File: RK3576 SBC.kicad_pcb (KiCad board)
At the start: 2 copper layers, 0 parts

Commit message: Add files via upload
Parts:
- added AE1: Antenna_Shield, Connector_Coaxial:U.FL_Molex_MCRF_73412-0110_Vertical, F.Cu at (230.8, 103.9)
- added C1: 22u, Capacitor_SMD:C_0603_1608Metric, F.Cu at (189.6, 96.3)
- added C10: 47u, Capacitor_SMD:C_0805_2012Metric, F.Cu at (209.8, 99.5)
- added C100: 1u, Capacitor_SMD:C_0402_1005Metric_Pad0.74x0.62mm_HandSolder, F.Cu at (232.4, 201.0)
- added C101: 1u, Capacitor_SMD:C_0402_1005Metric_Pad0.74x0.62mm_HandSolder, F.Cu at (232.4, 203.0)
- added C102: 1u, Capacitor_SMD:C_0402_1005Metric_Pad0.74x0.62mm_HandSolder, F.Cu at (232.4, 193.1)
- added C103: 1u, Capacitor_SMD:C_0402_1005Metric_Pad0.74x0.62mm_HandSolder, F.Cu at (232.4, 195.1)
- added C104: 1n, Capacitor_SMD:C_0402_1005Metric_Pad0.74x0.62mm_HandSolder, F.Cu at (232.4, 197.0)
- added C105: 1u, Capacitor_SMD:C_0402_1005Metric_Pad0.74x0.62mm_HandSolder, F.Cu at (161.2, 162.5)
- added C106: 1u, Capacitor_SMD:C_0402_1005Metric_Pad0.74x0.62mm_HandSolder, F.Cu at (161.2, 164.4)
- added C107: 1u, Capacitor_SMD:C_0402_1005Metric_Pad0.74x0.62mm_HandSolder, F.Cu at (161.2, 166.4)
- added C108: 1u, Capacitor_SMD:C_0402_1005Metric_Pad0.74x0.62mm_HandSolder, F.Cu at (161.2, 168.4)
- added C109: 1u, Capacitor_SMD:C_0402_1005Metric_Pad0.74x0.62mm_HandSolder, F.Cu at (161.2, 170.3)
- added C11: 2.2u, Capacitor_SMD:C_0402_1005Metric, F.Cu at (206.9, 115.0)
- added C110: 1u, Capacitor_SMD:C_0402_1005Metric_Pad0.74x0.62mm_HandSolder, F.Cu at (161.2, 172.3)
- added C111: 1u, Capacitor_SMD:C_0402_1005Metric_Pad0.74x0.62mm_HandSolder, F.Cu at (164.4, 162.5)
- added C112: 1u, Capacitor_SMD:C_0402_1005Metric_Pad0.74x0.62mm_HandSolder, F.Cu at (164.4, 164.4)
- added C113: 1u, Capacitor_SMD:C_0402_1005Metric_Pad0.74x0.62mm_HandSolder, F.Cu at (164.4, 166.4)
- added C114: 1u, Capacitor_SMD:C_0402_1005Metric_Pad0.74x0.62mm_HandSolder, F.Cu at (164.4, 168.4)
- added C115: 1u, Capacitor_SMD:C_0402_1005Metric_Pad0.74x0.62mm_HandSolder, F.Cu at (234.5, 140.4)
- added C116: 1u, Capacitor_SMD:C_0402_1005Metric_Pad0.74x0.62mm_HandSolder, F.Cu at (234.5, 142.3)
- added C117: 1u, Capacitor_SMD:C_0402_1005Metric_Pad0.74x0.62mm_HandSolder, F.Cu at (234.5, 144.3)
- added C118: 1u, Capacitor_SMD:C_0402_1005Metric_Pad0.74x0.62mm_HandSolder, F.Cu at (231.1, 162.9)
- added C119: 1u, Capacitor_SMD:C_0402_1005Metric_Pad0.74x0.62mm_HandSolder, F.Cu at (231.1, 164.8)
- added C12: 22u, Capacitor_SMD:C_0603_1608Metric, F.Cu at (193.6, 96.3)
- added C120: 1u, Capacitor_SMD:C_0201_0603Metric_Pad0.64x0.40mm_HandSolder, F.Cu at (127.8, 157.1)
- added C121: 1u, Capacitor_SMD:C_0402_1005Metric, F.Cu at (124.9, 150.8)
- added C122: 1u, Capacitor_SMD:C_0402_1005Metric, F.Cu at (124.9, 152.8)
- added C123: 22u, Capacitor_SMD:C_0603_1608Metric, F.Cu at (121.5, 151.1)
- added C124: 22u, Capacitor_SMD:C_0603_1608Metric, F.Cu at (121.5, 153.6)
- added C125: 22u, Capacitor_SMD:C_0603_1608Metric, F.Cu at (121.5, 156.1)
- added C126: 1u, Capacitor_SMD:C_0201_0603Metric_Pad0.64x0.40mm_HandSolder, F.Cu at (127.8, 158.8)
- added C127: 1u, Capacitor_SMD:C_0402_1005Metric, F.Cu at (124.9, 154.8)
- added C128: 1u, Capacitor_SMD:C_0402_1005Metric, F.Cu at (124.9, 156.8)
- added C129: 22u, Capacitor_SMD:C_0603_1608Metric, F.Cu at (121.5, 158.6)
- added C13: 22u, Capacitor_SMD:C_0603_1608Metric, F.Cu at (193.6, 98.8)
- added C130: 22u, Capacitor_SMD:C_0603_1608Metric, F.Cu at (121.5, 161.2)
- added C131: 22u, Capacitor_SMD:C_0603_1608Metric, F.Cu at (121.5, 163.7)
- added C132: 1u, Capacitor_SMD:C_0402_1005Metric, F.Cu at (124.9, 158.7)
- added C133: 1u, Capacitor_SMD:C_0402_1005Metric, F.Cu at (124.9, 160.7)
- added C134: 1u, Capacitor_SMD:C_0402_1005Metric, F.Cu at (124.9, 162.7)
- added C135: 1u, Capacitor_SMD:C_0402_1005Metric_Pad0.74x0.62mm_HandSolder, F.Cu at (222.0, 193.1)
- added C136: 1u, Capacitor_SMD:C_0402_1005Metric_Pad0.74x0.62mm_HandSolder, F.Cu at (222.0, 195.1)
- added C137: 1u, Capacitor_SMD:C_0402_1005Metric_Pad0.74x0.62mm_HandSolder, F.Cu at (222.0, 197.0)
- added C138: 1u, Capacitor_SMD:C_0402_1005Metric_Pad0.74x0.62mm_HandSolder, F.Cu at (222.0, 199.0)
- added C139: 1u, Capacitor_SMD:C_0402_1005Metric_Pad0.74x0.62mm_HandSolder, F.Cu at (222.0, 201.0)
- added C14: 22u, Capacitor_SMD:C_0603_1608Metric, F.Cu at (193.6, 101.3)
- added C140: 1u, Capacitor_SMD:C_0402_1005Metric_Pad0.74x0.62mm_HandSolder, F.Cu at (222.0, 202.9)
- added C141: 18pF, Capacitor_SMD:C_0402_1005Metric_Pad0.74x0.62mm_HandSolder, F.Cu at (222.0, 204.9)
- added C142: 18pF, Capacitor_SMD:C_0402_1005Metric_Pad0.74x0.62mm_HandSolder, F.Cu at (222.0, 206.9)
- added C143: 1u, Capacitor_SMD:C_0402_1005Metric_Pad0.74x0.62mm_HandSolder, F.Cu at (133.4, 160.7)
- added C144: 10u, Capacitor_SMD:C_0402_1005Metric_Pad0.74x0.62mm_HandSolder, F.Cu at (231.1, 150.9)
- added C145: 1u, Capacitor_SMD:C_0402_1005Metric_Pad0.74x0.62mm_HandSolder, F.Cu at (231.1, 152.8)
- added C146: 10u, Capacitor_SMD:C_0402_1005Metric_Pad0.74x0.62mm_HandSolder, F.Cu at (231.1, 154.8)
- added C147: 1u, Capacitor_SMD:C_0402_1005Metric_Pad0.74x0.62mm_HandSolder, F.Cu at (231.1, 156.8)
- added C148: 1u, Capacitor_SMD:C_0402_1005Metric_Pad0.74x0.62mm_HandSolder, F.Cu at (129.2, 199.3)
- added C149: 1u, Capacitor_SMD:C_0402_1005Metric_Pad0.74x0.62mm_HandSolder, F.Cu at (129.2, 201.3)
- added C15: 47u, Capacitor_SMD:C_0805_2012Metric, F.Cu at (209.8, 102.5)
- added C150: 1u, Capacitor_SMD:C_0402_1005Metric_Pad0.74x0.62mm_HandSolder, F.Cu at (129.2, 203.2)
- added C151: 1u, Capacitor_SMD:C_0402_1005Metric_Pad0.74x0.62mm_HandSolder, F.Cu at (129.2, 205.2)
- added C152: 1u, Capacitor_SMD:C_0402_1005Metric_Pad0.74x0.62mm_HandSolder, F.Cu at (129.2, 207.2)
- added C153: 1u, Capacitor_SMD:C_0402_1005Metric_Pad0.74x0.62mm_HandSolder, F.Cu at (129.2, 209.2)
- added C154: 1u, Capacitor_SMD:C_0402_1005Metric_Pad0.74x0.62mm_HandSolder, F.Cu at (132.4, 199.3)
- added C155: 1u, Capacitor_SMD:C_0402_1005Metric_Pad0.74x0.62mm_HandSolder, F.Cu at (132.4, 201.3)
- added C156: 1u, Capacitor_SMD:C_0402_1005Metric_Pad0.74x0.62mm_HandSolder, F.Cu at (132.4, 203.2)
- added C157: 1u, Capacitor_SMD:C_0402_1005Metric_Pad0.74x0.62mm_HandSolder, F.Cu at (132.4, 205.2)
- added C158: 1u, Capacitor_SMD:C_0402_1005Metric_Pad0.74x0.62mm_HandSolder, F.Cu at (132.4, 207.2)
- added C159: 1u, Capacitor_SMD:C_0402_1005Metric_Pad0.74x0.62mm_HandSolder, F.Cu at (133.4, 150.8)
- added C16: 2.2u, Capacitor_SMD:C_0402_1005Metric, F.Cu at (206.9, 117.0)
- added C160: 1u, Capacitor_SMD:C_0402_1005Metric_Pad0.74x0.62mm_HandSolder, F.Cu at (133.4, 152.8)
- added C161: 1u, Capacitor_SMD:C_0402_1005Metric_Pad0.74x0.62mm_HandSolder, F.Cu at (133.4, 154.8)
- added C162: 1u, Capacitor_SMD:C_0402_1005Metric_Pad0.74x0.62mm_HandSolder, F.Cu at (133.4, 156.8)
- added C163: 1u, Capacitor_SMD:C_0402_1005Metric_Pad0.74x0.62mm_HandSolder, F.Cu at (129.7, 193.0)
- added C164: 22u, Capacitor_SMD:C_0603_1608Metric, F.Cu at (130.0, 190.7)
- added C165: 1u, Capacitor_SMD:C_0201_0603Metric_Pad0.64x0.40mm_HandSolder, F.Cu at (142.7, 194.9)
- added C166: 1u, Capacitor_SMD:C_0201_0603Metric_Pad0.64x0.40mm_HandSolder, F.Cu at (142.7, 196.6)
- added C167: 1u, Capacitor_SMD:C_0201_0603Metric_Pad0.64x0.40mm_HandSolder, F.Cu at (142.7, 198.4)
- added C168: 200p, Capacitor_SMD:C_0402_1005Metric_Pad0.74x0.62mm_HandSolder, F.Cu at (151.6, 203.7)
- added C169: 200p, Capacitor_SMD:C_0402_1005Metric_Pad0.74x0.62mm_HandSolder, F.Cu at (151.6, 205.7)
- added C17: 22u, Capacitor_SMD:C_0603_1608Metric, F.Cu at (193.6, 103.8)
- added C170: 100n, Capacitor_SMD:C_0201_0603Metric_Pad0.64x0.40mm_HandSolder, F.Cu at (142.7, 200.1)
- added C171: 100n, Capacitor_SMD:C_0201_0603Metric_Pad0.64x0.40mm_HandSolder, F.Cu at (142.7, 201.9)
- added C172: 100n, Capacitor_SMD:C_0201_0603Metric_Pad0.64x0.40mm_HandSolder, F.Cu at (145.5, 194.9)
- added C173: 100n, Capacitor_SMD:C_0201_0603Metric_Pad0.64x0.40mm_HandSolder, F.Cu at (145.5, 196.6)
- added C174: 100n, Capacitor_SMD:C_0201_0603Metric_Pad0.64x0.40mm_HandSolder, F.Cu at (145.5, 198.4)
- added C175: 100n, Capacitor_SMD:C_0201_0603Metric_Pad0.64x0.40mm_HandSolder, F.Cu at (145.5, 200.1)
- added C176: 100n, Capacitor_SMD:C_0201_0603Metric_Pad0.64x0.40mm_HandSolder, F.Cu at (145.5, 201.9)
- added C177: 100n, Capacitor_SMD:C_0201_0603Metric_Pad0.64x0.40mm_HandSolder, F.Cu at (148.3, 194.9)
- added C178: 100n, Capacitor_SMD:C_0201_0603Metric_Pad0.64x0.40mm_HandSolder, F.Cu at (148.3, 196.6)
- added C179: 100n, Capacitor_SMD:C_0201_0603Metric_Pad0.64x0.40mm_HandSolder, F.Cu at (148.3, 198.4)
- added C18: 22u, Capacitor_SMD:C_0603_1608Metric, F.Cu at (193.6, 106.3)
- added C180: 1u, Capacitor_SMD:C_0402_1005Metric_Pad0.74x0.62mm_HandSolder, F.Cu at (160.5, 129.4)
- added C181: 22u, Capacitor_SMD:C_0603_1608Metric, F.Cu at (151.7, 201.0)
- added C182: 22u, Capacitor_SMD:C_0603_1608Metric, F.Cu at (169.3, 115.8)
- added C183: 1u, Capacitor_SMD:C_0402_1005Metric_Pad0.74x0.62mm_HandSolder, F.Cu at (151.6, 207.7)
- added C184: 100n, Capacitor_SMD:C_0201_0603Metric_Pad0.64x0.40mm_HandSolder, F.Cu at (160.3, 115.4)
- added C185: 100n, Capacitor_SMD:C_0201_0603Metric_Pad0.64x0.40mm_HandSolder, F.Cu at (160.3, 117.1)
- added C186: 100n, Capacitor_SMD:C_0201_0603Metric_Pad0.64x0.40mm_HandSolder, F.Cu at (160.3, 118.9)
- added C187: 100n, Capacitor_SMD:C_0201_0603Metric_Pad0.64x0.40mm_HandSolder, F.Cu at (160.3, 120.6)
- added C188: 100n, Capacitor_SMD:C_0201_0603Metric_Pad0.64x0.40mm_HandSolder, F.Cu at (160.3, 122.4)
- added C189: 100n, Capacitor_SMD:C_0201_0603Metric_Pad0.64x0.40mm_HandSolder, F.Cu at (160.3, 124.1)
- added C19: 22u, Capacitor_SMD:C_0603_1608Metric, F.Cu at (193.6, 108.8)
- added C190: 100n, Capacitor_SMD:C_0201_0603Metric_Pad0.64x0.40mm_HandSolder, F.Cu at (163.1, 115.4)
- added C191: 100n, Capacitor_SMD:C_0201_0603Metric_Pad0.64x0.40mm_HandSolder, F.Cu at (163.1, 117.1)
- added C196: 100n, Capacitor_SMD:C_0201_0603Metric_Pad0.64x0.40mm_HandSolder, F.Cu at (163.1, 118.9)
- added C197: 100n, Capacitor_SMD:C_0201_0603Metric_Pad0.64x0.40mm_HandSolder, F.Cu at (163.1, 120.6)
- added C198: 100n, Capacitor_SMD:C_0201_0603Metric_Pad0.64x0.40mm_HandSolder, F.Cu at (163.1, 122.4)
- added C199: 100n, Capacitor_SMD:C_0201_0603Metric_Pad0.64x0.40mm_HandSolder, F.Cu at (163.1, 124.1)
- added C2: 22u, Capacitor_SMD:C_0603_1608Metric, F.Cu at (189.6, 98.8)
- added C20: 47u, Capacitor_SMD:C_0805_2012Metric, F.Cu at (209.8, 105.5)
- added C200: 100n, Capacitor_SMD:C_0201_0603Metric_Pad0.64x0.40mm_HandSolder, F.Cu at (165.9, 115.4)
- added C201: 100n, Capacitor_SMD:C_0201_0603Metric_Pad0.64x0.40mm_HandSolder, F.Cu at (165.9, 117.1)
- added C202: 100n, Capacitor_SMD:C_0201_0603Metric_Pad0.64x0.40mm_HandSolder, F.Cu at (165.9, 118.9)
- added C203: 100n, Capacitor_SMD:C_0201_0603Metric_Pad0.64x0.40mm_HandSolder, F.Cu at (165.9, 120.6)
- added C204: 1u, Capacitor_SMD:C_0201_0603Metric_Pad0.64x0.40mm_HandSolder, F.Cu at (199.5, 169.6)
- added C205: 1u, Capacitor_SMD:C_0201_0603Metric_Pad0.64x0.40mm_HandSolder, F.Cu at (199.5, 171.4)
- added C206: 1u, Capacitor_SMD:C_0201_0603Metric_Pad0.64x0.40mm_HandSolder, F.Cu at (199.5, 173.1)
- added C207: 1u, Capacitor_SMD:C_0201_0603Metric_Pad0.64x0.40mm_HandSolder, F.Cu at (199.5, 174.9)
- added C208: 10u, Capacitor_SMD:C_0603_1608Metric, F.Cu at (208.5, 181.3)
- added C209: 1u, Capacitor_SMD:C_0201_0603Metric_Pad0.64x0.40mm_HandSolder, F.Cu at (199.5, 176.6)
- added C21: 2.2u, Capacitor_SMD:C_0402_1005Metric, F.Cu at (206.9, 118.9)
- added C210: 10u, Capacitor_SMD:C_0603_1608Metric, F.Cu at (208.5, 183.8)
- added C211: 1u, Capacitor_SMD:C_0201_0603Metric_Pad0.64x0.40mm_HandSolder, F.Cu at (199.5, 178.4)
- added C212: 1u, Capacitor_SMD:C_0201_0603Metric_Pad0.64x0.40mm_HandSolder, F.Cu at (199.5, 180.1)
- added C213: 1u, Capacitor_SMD:C_0201_0603Metric_Pad0.64x0.40mm_HandSolder, F.Cu at (202.3, 169.6)
- added C214: 1u, Capacitor_SMD:C_0201_0603Metric_Pad0.64x0.40mm_HandSolder, F.Cu at (202.3, 171.4)
- added C215: 1u, Capacitor_SMD:C_0201_0603Metric_Pad0.64x0.40mm_HandSolder, F.Cu at (202.3, 173.1)
- added C216: 1u, Capacitor_SMD:C_0201_0603Metric_Pad0.64x0.40mm_HandSolder, F.Cu at (202.3, 174.9)
- added C217: 1u, Capacitor_SMD:C_0201_0603Metric_Pad0.64x0.40mm_HandSolder, F.Cu at (202.3, 176.6)
- added C218: 1u, Capacitor_SMD:C_0201_0603Metric_Pad0.64x0.40mm_HandSolder, F.Cu at (202.3, 178.4)
- added C219: 1u, Capacitor_SMD:C_0201_0603Metric_Pad0.64x0.40mm_HandSolder, F.Cu at (202.3, 180.1)
- added C22: 2.2u, Capacitor_SMD:C_0402_1005Metric, F.Cu at (206.9, 120.9)
- added C220: 1u, Capacitor_SMD:C_0201_0603Metric_Pad0.64x0.40mm_HandSolder, F.Cu at (205.1, 169.6)
- added C221: 1u, Capacitor_SMD:C_0201_0603Metric_Pad0.64x0.40mm_HandSolder, F.Cu at (205.1, 171.4)
- added C222: 1u, Capacitor_SMD:C_0201_0603Metric_Pad0.64x0.40mm_HandSolder, F.Cu at (205.1, 173.1)
- added C223: 10u, Capacitor_SMD:C_0603_1608Metric, F.Cu at (208.5, 186.3)
- added C224: 10u, Capacitor_SMD:C_0603_1608Metric, F.Cu at (208.5, 188.9)
- added C225: 1u, Capacitor_SMD:C_0201_0603Metric_Pad0.64x0.40mm_HandSolder, F.Cu at (205.1, 174.9)
- added C226: 1u, Capacitor_SMD:C_0201_0603Metric_Pad0.64x0.40mm_HandSolder, F.Cu at (205.1, 176.6)
- added C227: 20pF, Capacitor_SMD:C_0402_1005Metric_Pad0.74x0.62mm_HandSolder, F.Cu at (215.2, 184.8)
- added C228: 20pF, Capacitor_SMD:C_0402_1005Metric_Pad0.74x0.62mm_HandSolder, F.Cu at (215.2, 186.8)
- added C229: 1u, Capacitor_SMD:C_0201_0603Metric_Pad0.64x0.40mm_HandSolder, F.Cu at (143.7, 140.3)
- added C23: 2.2u, Capacitor_SMD:C_0402_1005Metric, F.Cu at (209.7, 111.0)
- added C230: 1u, Capacitor_SMD:C_0201_0603Metric_Pad0.64x0.40mm_HandSolder, F.Cu at (143.7, 142.0)
- added C231: 1u, Capacitor_SMD:C_0201_0603Metric_Pad0.64x0.40mm_HandSolder, F.Cu at (143.7, 143.8)
- added C232: 1u, Capacitor_SMD:C_0201_0603Metric_Pad0.64x0.40mm_HandSolder, F.Cu at (143.7, 145.5)
- added C233: 1u, Capacitor_SMD:C_0201_0603Metric_Pad0.64x0.40mm_HandSolder, F.Cu at (143.7, 147.3)
- added C234: 1u, Capacitor_SMD:C_0201_0603Metric_Pad0.64x0.40mm_HandSolder, F.Cu at (143.7, 149.0)
- added C235: 1u, Capacitor_SMD:C_0201_0603Metric_Pad0.64x0.40mm_HandSolder, F.Cu at (143.7, 150.8)
- added C236: 1u, Capacitor_SMD:C_0201_0603Metric_Pad0.64x0.40mm_HandSolder, F.Cu at (143.7, 152.5)
- added C237: 1u, Capacitor_SMD:C_0201_0603Metric_Pad0.64x0.40mm_HandSolder, F.Cu at (143.7, 154.3)
- added C238: 1u, Capacitor_SMD:C_0201_0603Metric_Pad0.64x0.40mm_HandSolder, F.Cu at (143.7, 156.0)
- added C239: 1u, Capacitor_SMD:C_0201_0603Metric_Pad0.64x0.40mm_HandSolder, F.Cu at (143.7, 157.8)
- added C24: 2.2u, Capacitor_SMD:C_0402_1005Metric, F.Cu at (209.7, 113.0)
- added C240: 22u, Capacitor_SMD:C_0603_1608Metric, F.Cu at (140.3, 140.6)
- added C241: 22u, Capacitor_SMD:C_0603_1608Metric, F.Cu at (140.3, 143.2)
- added C242: 22u, Capacitor_SMD:C_0603_1608Metric, F.Cu at (140.3, 145.7)
- added C243: 1u, Capacitor_SMD:C_0201_0603Metric_Pad0.64x0.40mm_HandSolder, F.Cu at (146.5, 140.3)
- added C244: 1u, Capacitor_SMD:C_0201_0603Metric_Pad0.64x0.40mm_HandSolder, F.Cu at (146.5, 142.0)
- added C245: 1u, Capacitor_SMD:C_0201_0603Metric_Pad0.64x0.40mm_HandSolder, F.Cu at (146.5, 143.8)
- added C246: 1u, Capacitor_SMD:C_0201_0603Metric_Pad0.64x0.40mm_HandSolder, F.Cu at (146.5, 145.5)
- added C247: 1u, Capacitor_SMD:C_0201_0603Metric_Pad0.64x0.40mm_HandSolder, F.Cu at (146.5, 147.3)
- added C248: 1u, Capacitor_SMD:C_0201_0603Metric_Pad0.64x0.40mm_HandSolder, F.Cu at (146.5, 149.0)
- added C249: 1u, Capacitor_SMD:C_0201_0603Metric_Pad0.64x0.40mm_HandSolder, F.Cu at (146.5, 150.8)
- added C25: 22u, Capacitor_SMD:C_0603_1608Metric, F.Cu at (197.6, 96.3)
- added C250: 1u, Capacitor_SMD:C_0201_0603Metric_Pad0.64x0.40mm_HandSolder, F.Cu at (146.5, 152.5)
- added C251: 1u, Capacitor_SMD:C_0201_0603Metric_Pad0.64x0.40mm_HandSolder, F.Cu at (146.5, 154.3)
- added C252: 1u, Capacitor_SMD:C_0201_0603Metric_Pad0.64x0.40mm_HandSolder, F.Cu at (146.5, 156.0)
- added C253: 1u, Capacitor_SMD:C_0201_0603Metric_Pad0.64x0.40mm_HandSolder, F.Cu at (146.5, 157.8)
- added C254: 1u, Capacitor_SMD:C_0201_0603Metric_Pad0.64x0.40mm_HandSolder, F.Cu at (149.3, 140.3)
- added C255: 1u, Capacitor_SMD:C_0201_0603Metric_Pad0.64x0.40mm_HandSolder, F.Cu at (149.3, 142.0)
- added C256: 1u, Capacitor_SMD:C_0201_0603Metric_Pad0.64x0.40mm_HandSolder, F.Cu at (149.3, 143.8)
- added C257: 22u, Capacitor_SMD:C_0603_1608Metric, F.Cu at (140.3, 148.2)
- added C258: 1u, Capacitor_SMD:C_0201_0603Metric_Pad0.64x0.40mm_HandSolder, F.Cu at (149.3, 145.5)
- added C259: 1u, Capacitor_SMD:C_0201_0603Metric_Pad0.64x0.40mm_HandSolder, F.Cu at (149.3, 147.3)
- added C26: 22u, Capacitor_SMD:C_0603_1608Metric, F.Cu at (197.6, 98.8)
- added C260: 1u, Capacitor_SMD:C_0201_0603Metric_Pad0.64x0.40mm_HandSolder, F.Cu at (149.3, 149.0)
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
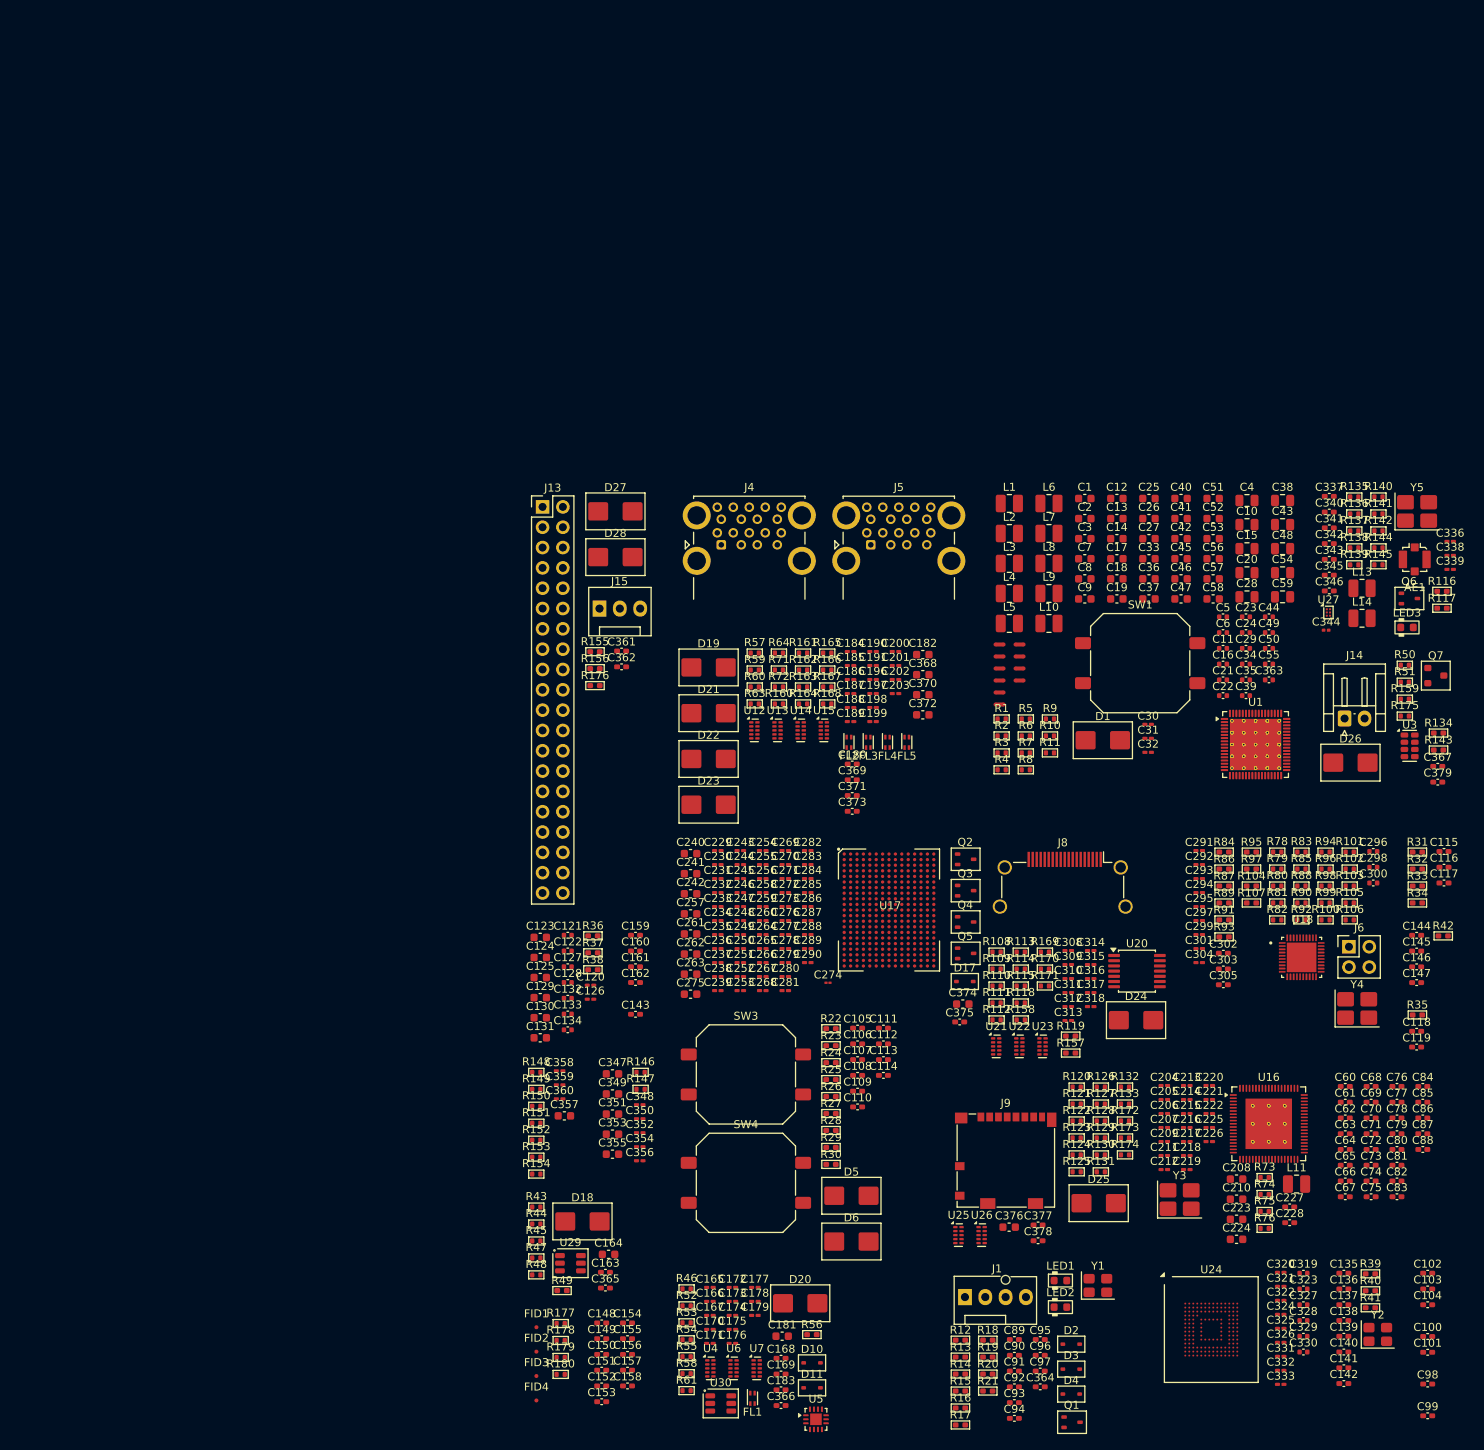
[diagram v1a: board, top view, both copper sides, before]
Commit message: SBC Board V0.2
The SBC schematics before footprint and part number check
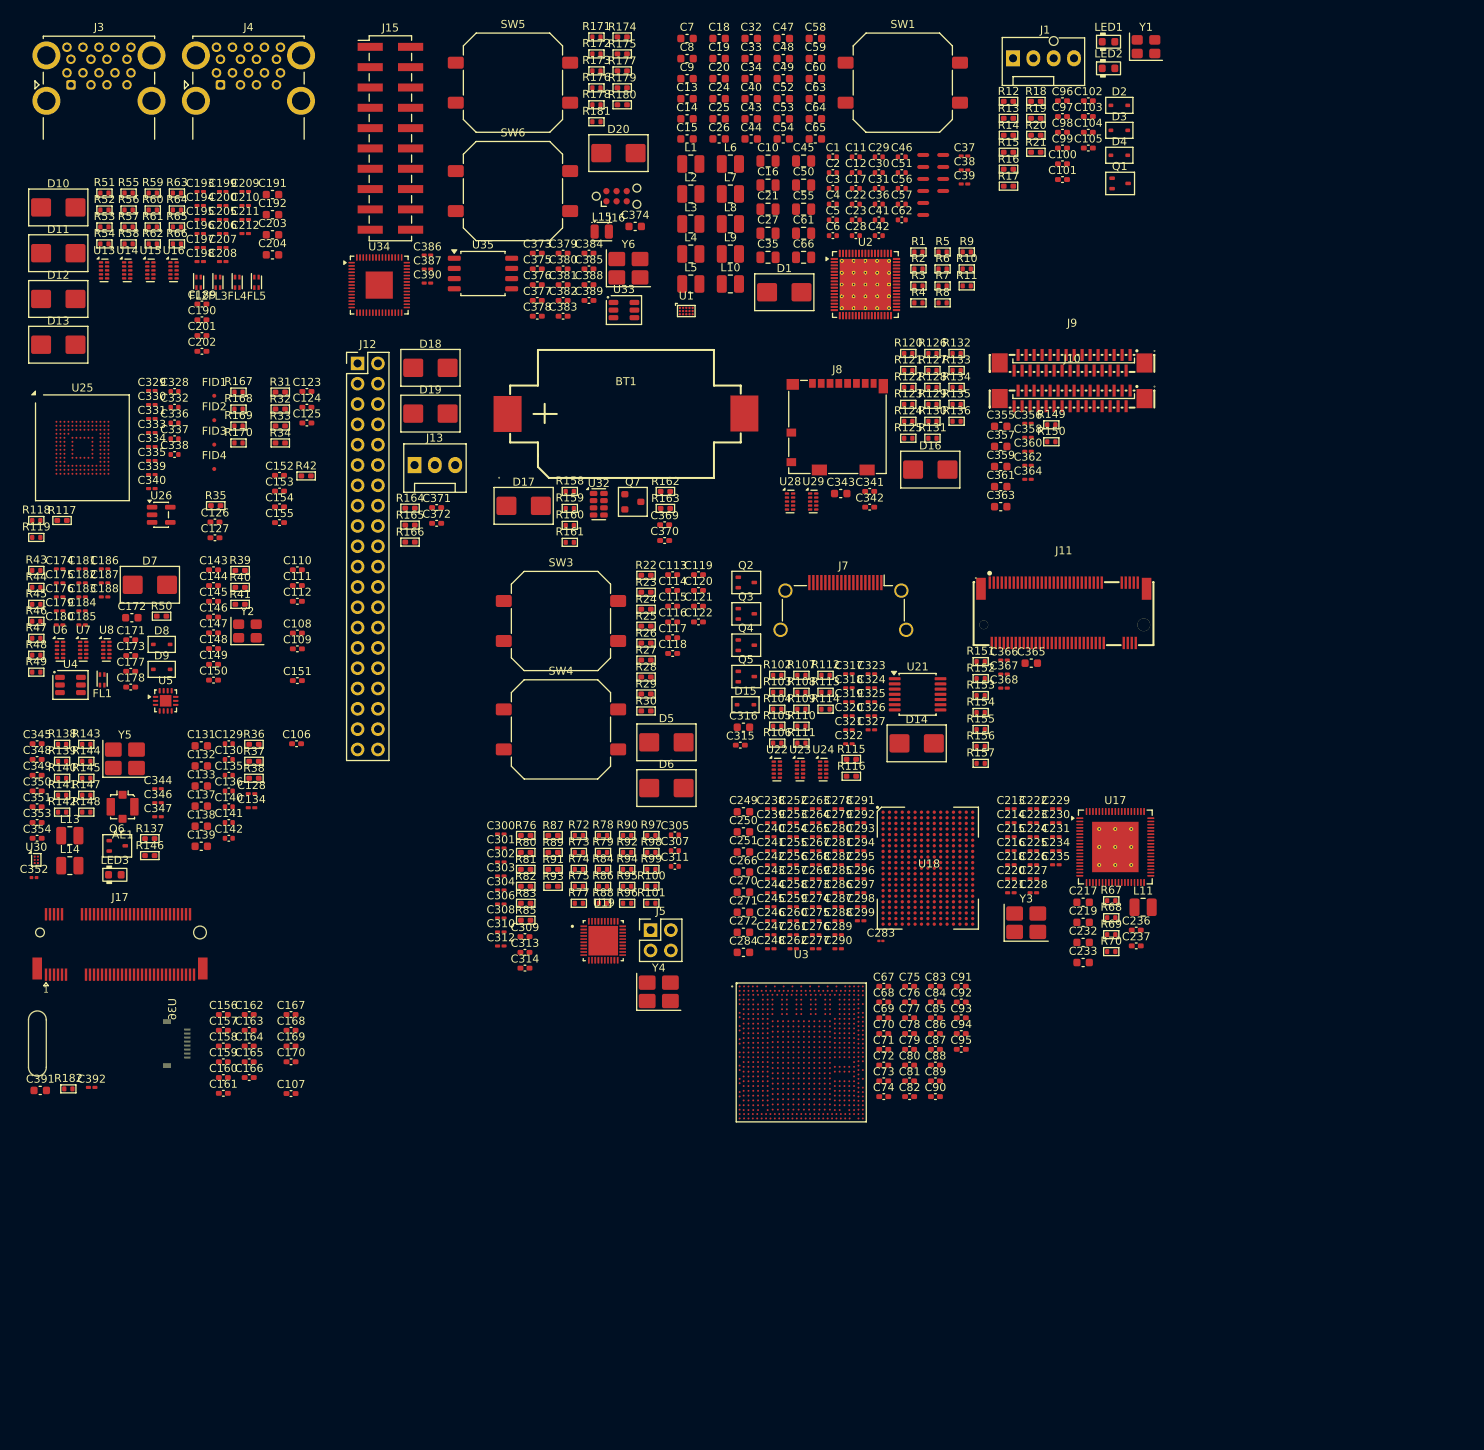
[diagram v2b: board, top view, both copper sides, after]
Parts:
- removed D21, D22, D23, D24, D25, D26, D27, D28: SMBJ5.0CA, PCM_Diode_SMD_AKL:D_SMB_TVS
- removed J14: B2B Connector, Connector_JST:JST_EH_S2B-EH_1x02_P2.50mm_Horizontal
- removed J6: POE Connector, Connector_PinHeader_2.54mm:PinHeader_2x02_P2.54mm_Vertical
- removed R71: 0R, PCM_Resistor_SMD_AKL:R_0402_1005Metric
- removed U12: TPD4E05U06DQA, Package_SON:USON-10_2.5x1.0mm_P0.5mm
- removed U20: TXB0104PW, Package_SO:TSSOP-14_4.4x5mm_P0.65mm
- removed U27: BGS12P2L6E6327XTSA1, Package_LGA:Infineon_PG-TSNP-6-10_0.7x1.1mm_0.7x1.1mm_P0.4mm
- added BT1: BS-06-B4AA012, easyeda2kicad:BAT-SMD_BS-06-B4AA012, F.Cu at (132.2, 85.7)
- added C192: 22u, Capacitor_SMD:C_0603_1608Metric, F.Cu at (88.0, 60.8)
- added C193: 100n, Capacitor_SMD:C_0201_0603Metric_Pad0.64x0.40mm_HandSolder, F.Cu at (79.0, 57.9)
- added C194: 100n, Capacitor_SMD:C_0201_0603Metric_Pad0.64x0.40mm_HandSolder, F.Cu at (79.0, 59.6)
- added C195: 100n, Capacitor_SMD:C_0201_0603Metric_Pad0.64x0.40mm_HandSolder, F.Cu at (79.0, 61.4)
- added C306: 1u, Capacitor_SMD:C_0201_0603Metric_Pad0.64x0.40mm_HandSolder, F.Cu at (116.6, 146.9)
- added C307: 10u, Capacitor_SMD:C_0402_1005Metric, F.Cu at (138.3, 140.3)
- added C334: 1u, Capacitor_SMD:C_0201_0603Metric_Pad0.64x0.40mm_HandSolder, F.Cu at (73.0, 89.8)
- added C335: 1u, Capacitor_SMD:C_0201_0603Metric_Pad0.64x0.40mm_HandSolder, F.Cu at (73.0, 91.5)
- added C380: 1u, Capacitor_SMD:C_0402_1005Metric_Pad0.74x0.62mm_HandSolder, F.Cu at (124.4, 67.6)
- added C381: 1u, Capacitor_SMD:C_0402_1005Metric_Pad0.74x0.62mm_HandSolder, F.Cu at (124.4, 69.5)
- added C382: 1u, Capacitor_SMD:C_0402_1005Metric_Pad0.74x0.62mm_HandSolder, F.Cu at (124.4, 71.5)
- added C383: 1u, Capacitor_SMD:C_0402_1005Metric_Pad0.74x0.62mm_HandSolder, F.Cu at (124.4, 73.5)
- added C384: 1u, Capacitor_SMD:C_0402_1005Metric_Pad0.74x0.62mm_HandSolder, F.Cu at (127.6, 65.6)
- added C385: 1u, Capacitor_SMD:C_0402_1005Metric_Pad0.74x0.62mm_HandSolder, F.Cu at (127.6, 67.6)
- added C386: 1u, Capacitor_SMD:C_0201_0603Metric_Pad0.64x0.40mm_HandSolder, F.Cu at (107.4, 65.8)
- added C387: 1u, Capacitor_SMD:C_0201_0603Metric_Pad0.64x0.40mm_HandSolder, F.Cu at (107.4, 67.6)
- added C388: 34pF, Capacitor_SMD:C_0402_1005Metric_Pad0.74x0.62mm_HandSolder, F.Cu at (127.6, 69.5)
- added C389: 34pF, Capacitor_SMD:C_0402_1005Metric_Pad0.74x0.62mm_HandSolder, F.Cu at (127.6, 71.5)
- added C390: 1u, Capacitor_SMD:C_0201_0603Metric_Pad0.64x0.40mm_HandSolder, F.Cu at (107.4, 69.3)
- added C391: 10u, Capacitor_SMD:C_0603_1608Metric, F.Cu at (59.0, 170.2)
- added C392: 1u, Capacitor_SMD:C_0201_0603Metric_Pad0.64x0.40mm_HandSolder, F.Cu at (65.4, 169.9)
- added D12: SMBJ5.0CA, PCM_Diode_SMD_AKL:D_SMB_TVS, F.Cu at (61.3, 71.3)
- added D13: SMBJ5.0CA, PCM_Diode_SMD_AKL:D_SMB_TVS, F.Cu at (61.3, 77.0)
- added D14: SMBJ5.0CA, PCM_Diode_SMD_AKL:D_SMB_TVS, F.Cu at (168.6, 126.9)
- added D15: PESD5V0S1BA, PCM_Diode_SMD_AKL:D_SOD-323_TVS, F.Cu at (147.2, 122.0)
- added D16: SMBJ5.0CA, PCM_Diode_SMD_AKL:D_SMB_TVS, F.Cu at (170.3, 92.6)
- added D7: SMBJ5.0CA, PCM_Diode_SMD_AKL:D_SMB_TVS, F.Cu at (72.7, 107.0)
- added D8: PESD5V0S1BA, PCM_Diode_SMD_AKL:D_SOD-323_TVS, F.Cu at (74.2, 114.5)
- added D9: PESD5V0S1BA, PCM_Diode_SMD_AKL:D_SOD-323_TVS, F.Cu at (74.2, 117.6)
- added J10: DSI Connector, easyeda2kicad:FPC-SMD_30P-L20.5-W2.0-P0.50, F.Cu at (188.0, 83.8)
- added J11: 1-2199230-5, easyeda2kicad:PCIE-SMD_75P-P0.50_1-2199230-5, F.Cu at (186.9, 110.5)
- added J12: Raspberry_Pi_4, #kicad Library:40-pin GPIO Header for Raspberry Pi, F.Cu at (98.7, 79.4)
- added J16: Conn_ARM_SWD_TagConnect_TC2030-NL, Connector:Tag-Connect_TC2030-IDC-NL_2x03_P1.27mm_Vertical, F.Cu at (131.0, 58.5)
- added J17: TE_2199230-3, Datasheet_Footprints:TE_2199230-3, F.Cu at (69.0, 150.5)
- added J3: USB3_A_Stacked, Connector_USB:USB3_A_Molex_48406-0001_Horizontal_Stacked, F.Cu at (62.8, 44.5)
- added J7: HDMI_A, Connector_Video:HDMI_A_Amphenol_10029449-x01xLF_Horizontal, F.Cu at (159.4, 111.8)
- added L15: YL201209-3R3K, Inductor_SMD:L_Coilcraft_0805HQ_2012Metric, F.Cu at (129.2, 62.9)
- added R181: 1k, PCM_Resistor_SMD_AKL:R_0402_1005Metric, F.Cu at (128.5, 49.2)
- added R182: 10k, PCM_Resistor_SMD_AKL:R_0402_1005Metric, F.Cu at (62.5, 170.1)
- added R62: 100k, PCM_Resistor_SMD_AKL:R_0402_1005Metric, F.Cu at (73.1, 64.4)
- added R65: 0R, PCM_Resistor_SMD_AKL:R_0402_1005Metric, F.Cu at (76.1, 62.3)
- added R66: 0R, PCM_Resistor_SMD_AKL:R_0402_1005Metric, F.Cu at (76.1, 64.4)
- added R67: 100k, PCM_Resistor_SMD_AKL:R_0402_1005Metric, F.Cu at (192.9, 146.5)
- added R68: 100k, PCM_Resistor_SMD_AKL:R_0402_1005Metric, F.Cu at (192.9, 148.7)
- added R69: 0R, PCM_Resistor_SMD_AKL:R_0402_1005Metric, F.Cu at (192.9, 150.8)
- added R70: 6.2k, PCM_Resistor_SMD_AKL:R_0402_1005Metric, F.Cu at (192.9, 152.9)
- added R77: 4.7k, PCM_Resistor_SMD_AKL:R_0402_1005Metric, F.Cu at (126.3, 146.8)
- added SW5: SW_Push, Button_Switch_SMD:SW_Push_1P1T_NO_CK_PTS125Sx85SMTR, F.Cu at (118.1, 44.3)
- added SW6: SW_Push, Button_Switch_SMD:SW_Push_1P1T_NO_CK_PTS125Sx85SMTR, F.Cu at (118.1, 57.8)
- added U19: RTL8211F-CG, #kicad Library:QFN40P500X500X90-41N, F.Cu at (129.4, 151.5)
- added U2: RK806S-5, Package_DFN_QFN:QFN-68-1EP_8x8mm_P0.4mm_EP6.4x6.4mm_ThermalVias, F.Cu at (162.2, 69.5)
- added U28: TPD4E05U06DQA, Package_SON:USON-10_2.5x1.0mm_P0.5mm, F.Cu at (152.7, 96.6)
- added U32: RV-3028-C7, Package_SON:MicroCrystal_C7_SON-8_1.5x3.2mm_P0.9mm, F.Cu at (128.8, 97.0)
- added U33: ETA7014S2G, PCM_Package_TO_SOT_SMD_AKL:TSOT-23-6, F.Cu at (132.0, 72.7)
- added U34: RP2350A, Package_DFN_QFN:QFN-60-1EP_7x7mm_P0.4mm_EP3.4x3.4mm, F.Cu at (101.4, 69.6)
- added U35: W25Q128JVS, Package_SO:SOIC-8_5.3x5.3mm_P1.27mm, F.Cu at (114.3, 68.1)
- added U36: 0.96 OLED Display 8 pins, Datasheet_Footprints:FFC-SMD_8P-P0.50_AFC42-S08FMA-1H_BOTTOM, F.Cu at (75.5, 164.4)
- added U8: TPD4E05U06DQA, Package_SON:USON-10_2.5x1.0mm_P0.5mm, F.Cu at (67.3, 115.2)
- added Y6: TAXM12M4RLBDDT2T, Crystal:Crystal_SMD_3225-4Pin_3.2x2.5mm_HandSoldering, F.Cu at (132.5, 67.5)
- C1, C12, C17, C2, C3, C36, C41, C42, C46, C51, C56, C57: value 22u -> 2.2u; footprint Capacitor_SMD:C_0603_1608Metric -> Capacitor_SMD:C_0402_1005Metric
- C100, C99: value 1u -> 12pF
- C104: value 1n -> 1u
- C112: value 1u -> 1n
- C120, C126, C165, C166, C167, C348: footprint Capacitor_SMD:C_0201_0603Metric_Pad0.64x0.40mm_HandSolder -> Capacitor_SMD:C_0402_1005Metric_Pad0.74x0.62mm_HandSolder
- C121, C122, C127: footprint Capacitor_SMD:C_0402_1005Metric -> Capacitor_SMD:C_0402_1005Metric_Pad0.74x0.62mm_HandSolder
- C123, C124, C125, C164, C370, C376: value 22u -> 1u; footprint Capacitor_SMD:C_0603_1608Metric -> Capacitor_SMD:C_0402_1005Metric_Pad0.74x0.62mm_HandSolder
- C128, C134: footprint Capacitor_SMD:C_0402_1005Metric -> Capacitor_SMD:C_0201_0603Metric_Pad0.64x0.40mm_HandSolder
- C129, C130: value 22u -> 1u; footprint Capacitor_SMD:C_0603_1608Metric -> Capacitor_SMD:C_0402_1005Metric
- C132, C133: value 1u -> 22u; footprint Capacitor_SMD:C_0402_1005Metric -> Capacitor_SMD:C_0603_1608Metric
- C135, C136, C140: footprint Capacitor_SMD:C_0402_1005Metric_Pad0.74x0.62mm_HandSolder -> Capacitor_SMD:C_0402_1005Metric
- C137, C138, C139, C365, C63, C64, C65: value 1u -> 22u; footprint Capacitor_SMD:C_0402_1005Metric_Pad0.74x0.62mm_HandSolder -> Capacitor_SMD:C_0603_1608Metric
- C141, C142: value 18pF -> 1u; footprint Capacitor_SMD:C_0402_1005Metric_Pad0.74x0.62mm_HandSolder -> Capacitor_SMD:C_0402_1005Metric
- C144, C146, C70, C71, C72, C80, C88: value 10u -> 1u
- C149, C150: value 1u -> 18pF
- C15, C20, C43, C48, C54, C59: value 47u -> 22u; footprint Capacitor_SMD:C_0805_2012Metric -> Capacitor_SMD:C_0603_1608Metric
- C152, C154, C67, C77, C78, C86, C87, C95: value 1u -> 10u
- C16, C21, C35, C50, C55: value 2.2u -> 47u; footprint Capacitor_SMD:C_0402_1005Metric -> Capacitor_SMD:C_0805_2012Metric
- C168, C169: value 200p -> 1u
- C170, C171, C173, C189, C190, C201, C202: value 100n -> 1u; footprint Capacitor_SMD:C_0201_0603Metric_Pad0.64x0.40mm_HandSolder -> Capacitor_SMD:C_0402_1005Metric_Pad0.74x0.62mm_HandSolder
- C172, C191, C203: value 100n -> 22u; footprint Capacitor_SMD:C_0201_0603Metric_Pad0.64x0.40mm_HandSolder -> Capacitor_SMD:C_0603_1608Metric
- C174, C175, C176: value 100n -> 1u
- C177, C178: value 100n -> 200p; footprint Capacitor_SMD:C_0201_0603Metric_Pad0.64x0.40mm_HandSolder -> Capacitor_SMD:C_0402_1005Metric_Pad0.74x0.62mm_HandSolder
- C180, C183: value 1u -> 100n; footprint Capacitor_SMD:C_0402_1005Metric_Pad0.74x0.62mm_HandSolder -> Capacitor_SMD:C_0201_0603Metric_Pad0.64x0.40mm_HandSolder
- C181, C182: value 22u -> 100n; footprint Capacitor_SMD:C_0603_1608Metric -> Capacitor_SMD:C_0201_0603Metric_Pad0.64x0.40mm_HandSolder
- C204, C249, C250, C251, C266, C270, C271, C272, C284, C359: value 1u -> 22u; footprint Capacitor_SMD:C_0201_0603Metric_Pad0.64x0.40mm_HandSolder -> Capacitor_SMD:C_0603_1608Metric
- C205, C206, C207, C209, C211, C212: value 1u -> 100n
- C208, C210: value 10u -> 100n; footprint Capacitor_SMD:C_0603_1608Metric -> Capacitor_SMD:C_0201_0603Metric_Pad0.64x0.40mm_HandSolder
- C217, C219, C232, C233: value 1u -> 10u; footprint Capacitor_SMD:C_0201_0603Metric_Pad0.64x0.40mm_HandSolder -> Capacitor_SMD:C_0603_1608Metric
- C223: footprint Capacitor_SMD:C_0603_1608Metric -> Capacitor_SMD:C_0201_0603Metric_Pad0.64x0.40mm_HandSolder
- C224: value 10u -> 1u; footprint Capacitor_SMD:C_0603_1608Metric -> Capacitor_SMD:C_0201_0603Metric_Pad0.64x0.40mm_HandSolder
- C227, C228: value 20pF -> 1u; footprint Capacitor_SMD:C_0402_1005Metric_Pad0.74x0.62mm_HandSolder -> Capacitor_SMD:C_0201_0603Metric_Pad0.64x0.40mm_HandSolder
- C236, C237: value 1u -> 20pF; footprint Capacitor_SMD:C_0201_0603Metric_Pad0.64x0.40mm_HandSolder -> Capacitor_SMD:C_0402_1005Metric_Pad0.74x0.62mm_HandSolder
- C24, C34, C363, C44, C49: value 2.2u -> 22u; footprint Capacitor_SMD:C_0402_1005Metric -> Capacitor_SMD:C_0603_1608Metric
- C240, C241, C242, C257, C261, C262, C263, C275, C347, C368, C37: value 22u -> 1u; footprint Capacitor_SMD:C_0603_1608Metric -> Capacitor_SMD:C_0201_0603Metric_Pad0.64x0.40mm_HandSolder
- C27, C45: value 22u -> 47u; footprint Capacitor_SMD:C_0603_1608Metric -> Capacitor_SMD:C_0805_2012Metric
- C274: footprint Capacitor_SMD:C_01005_0402Metric -> Capacitor_SMD:C_0201_0603Metric_Pad0.64x0.40mm_HandSolder
- C28, C4: value 47u -> 2.2u; footprint Capacitor_SMD:C_0805_2012Metric -> Capacitor_SMD:C_0402_1005Metric
- C283: footprint Capacitor_SMD:C_0201_0603Metric_Pad0.64x0.40mm_HandSolder -> Capacitor_SMD:C_01005_0402Metric
- C296, C298, C300, C330: value 10u -> 1u; footprint Capacitor_SMD:C_0402_1005Metric -> Capacitor_SMD:C_0201_0603Metric_Pad0.64x0.40mm_HandSolder
- C30, C336, C338: value 1u -> 2.2u; footprint Capacitor_SMD:C_0201_0603Metric_Pad0.64x0.40mm_HandSolder -> Capacitor_SMD:C_0402_1005Metric
- C302, C303: value 18pF -> 1u; footprint Capacitor_SMD:C_0402_1005Metric_Pad0.74x0.62mm_HandSolder -> Capacitor_SMD:C_0201_0603Metric_Pad0.64x0.40mm_HandSolder
- C305: value 1u -> 10u; footprint Capacitor_SMD:C_0402_1005Metric_Pad0.74x0.62mm_HandSolder -> Capacitor_SMD:C_0402_1005Metric
- C308, C310, C312: value 220n -> 1u
- C309, C315: value 220n -> 1u; footprint Capacitor_SMD:C_0201_0603Metric_Pad0.64x0.40mm_HandSolder -> Capacitor_SMD:C_0402_1005Metric_Pad0.74x0.62mm_HandSolder
- C31: value 10n -> 2.2u; footprint Capacitor_SMD:C_0201_0603Metric_Pad0.64x0.40mm_HandSolder -> Capacitor_SMD:C_0402_1005Metric
- C311: value 220n -> 10u; footprint Capacitor_SMD:C_0201_0603Metric_Pad0.64x0.40mm_HandSolder -> Capacitor_SMD:C_0402_1005Metric
- C313, C314: value 220n -> 18pF; footprint Capacitor_SMD:C_0201_0603Metric_Pad0.64x0.40mm_HandSolder -> Capacitor_SMD:C_0402_1005Metric_Pad0.74x0.62mm_HandSolder
- C316: value 220n -> 22u; footprint Capacitor_SMD:C_0201_0603Metric_Pad0.64x0.40mm_HandSolder -> Capacitor_SMD:C_0603_1608Metric
- C317, C318, C320, C321, C322, C324, C325: value 1u -> 220n
- C319, C323: value 10u -> 220n; footprint Capacitor_SMD:C_0402_1005Metric -> Capacitor_SMD:C_0201_0603Metric_Pad0.64x0.40mm_HandSolder
- C32: value 10n -> 22u; footprint Capacitor_SMD:C_0201_0603Metric_Pad0.64x0.40mm_HandSolder -> Capacitor_SMD:C_0603_1608Metric
- C327, C329: value 2.2u -> 1u; footprint Capacitor_SMD:C_0402_1005Metric -> Capacitor_SMD:C_0201_0603Metric_Pad0.64x0.40mm_HandSolder
- C328: value 2.2u -> 10u
- C332: value 1u -> 10u; footprint Capacitor_SMD:C_0201_0603Metric_Pad0.64x0.40mm_HandSolder -> Capacitor_SMD:C_0402_1005Metric
- C337, C62: value 1u -> 2.2u; footprint Capacitor_SMD:C_0402_1005Metric_Pad0.74x0.62mm_HandSolder -> Capacitor_SMD:C_0402_1005Metric
- C340, C364, C366, C367: footprint Capacitor_SMD:C_0402_1005Metric_Pad0.74x0.62mm_HandSolder -> Capacitor_SMD:C_0201_0603Metric_Pad0.64x0.40mm_HandSolder
- C341, C342: value DNP -> 1u
- C343: value 8p -> 22u; footprint Capacitor_SMD:C_0402_1005Metric_Pad0.74x0.62mm_HandSolder -> Capacitor_SMD:C_0603_1608Metric
- C344: value 10u -> 1u; footprint Capacitor_SMD:C_0201_0603Metric -> Capacitor_SMD:C_0201_0603Metric_Pad0.64x0.40mm_HandSolder
- C345: value 10pF -> 1u
- C346: value 10pF -> 1u; footprint Capacitor_SMD:C_0402_1005Metric_Pad0.74x0.62mm_HandSolder -> Capacitor_SMD:C_0201_0603Metric_Pad0.64x0.40mm_HandSolder
- C349: value 22u -> DNP; footprint Capacitor_SMD:C_0603_1608Metric -> Capacitor_SMD:C_0402_1005Metric_Pad0.74x0.62mm_HandSolder
- C350: value 1u -> DNP; footprint Capacitor_SMD:C_0201_0603Metric_Pad0.64x0.40mm_HandSolder -> Capacitor_SMD:C_0402_1005Metric_Pad0.74x0.62mm_HandSolder
- C351: value 22u -> 8p; footprint Capacitor_SMD:C_0603_1608Metric -> Capacitor_SMD:C_0402_1005Metric_Pad0.74x0.62mm_HandSolder
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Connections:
- C1 pad 1: +5v -> Vbus_USB_{OTG}
- C10 pad 1: VDD_NPU_S0 -> VDD_CPU_BIG_S0
- C100 pad 1: VCCA_1V8_S3 -> Net-(U3GPIO0-OSC_XIN)
- C101 pad 1: VCCA_1V8_S3 -> VDDA_0.75v_S0
- C102 pad 1: VCC_3V3_S0 -> VCCA_1.8v_S0
- C103 pad 1: VCC_3V3_S0 -> VCC_3.3v_S0
- C104 pad 1: /RK3576/GPIO4/HDMI_HPD -> VDD_3.3v_S3
- C105 pad 1: VCCA_1V8_S0 -> VDD_3.3v_S3
- C106 pad 1: VDDA_0V75_S0 -> VCCA_1V8_S0
- C107 pad 1: /RK3576/SARADC/SARADC_VIN0_BOOT -> VCC_3V3_S0
- C108 pad 1: /RK3576/SARADC/SARADC_VIN1_KEY/RECOVERY -> VCCA_1V8_S3
- C109 pad 1: /RK3576/SARADC/SARADC_VIN2_HW_ID -> VCCA_1V8_S3
- C11 pad 1: VCCA1V8_PLDO2_S0 -> VCC_2V0_PLDO_S3
- C110 pad 1: /RK3576/SARADC/SARADC_VIN3_HP_HOOK -> VCC_3V3_S0
- C111 pad 1: /RK3576/SARADC/SARADC_VIN4_IN -> VCC_3V3_S0
- C112 pad 1: /RK3576/SARADC/SARADC_VIN5_BOM_ID -> /RK3576/GPIO4/HDMI_HPD
- C113 pad 1: /RK3576/SARADC/SARADC_VIN6 -> VCCA_1V8_S0
- C114 pad 1: /RK3576/SARADC/SARADC_VIN7_DC -> VDDA_0V75_S0
- C115 pad 1: VDDA_0V75_S0 -> /RK3576/SARADC/SARADC_VIN0_BOOT
- C116 pad 1: VCCA_1V8_S0 -> /RK3576/SARADC/SARADC_VIN1_KEY/RECOVERY
- C117 pad 1: VCC_3V3_S0 -> /RK3576/SARADC/SARADC_VIN2_HW_ID
- C118 pad 1: VDDA_0V85_S0 -> /RK3576/SARADC/SARADC_VIN3_HP_HOOK
- C119 pad 1: VCCA_1V8_S0 -> /RK3576/SARADC/SARADC_VIN4_IN
- C12 pad 1: +5v -> VCCA_1V8_S0
- C120 pad 1: VDDQ_DDR_S0 -> /RK3576/SARADC/SARADC_VIN5_BOM_ID
- C121 pad 1: VDDQ_DDR_S0 -> /RK3576/SARADC/SARADC_VIN6
- C122 pad 1: VDDQ_DDR_S0 -> /RK3576/SARADC/SARADC_VIN7_DC
- C123 pad 1: VDDQ_DDR_S0 -> VDDA_0V75_S0
- C124 pad 1: VDDQ_DDR_S0 -> VCCA_1V8_S0
- C125 pad 1: VDDQ_DDR_S0 -> VCC_3V3_S0
- C126 pad 1: VDD_DDR_S0 -> VDDA_0V85_S0
- C127 pad 1: VDD_DDR_S0 -> VCCA_1V8_S0
- C128 pad 1: VDD_DDR_S0 -> VDDQ_DDR_S0
- C129 pad 1: VDD_DDR_S0 -> VDDQ_DDR_S0
- C13 pad 1: VDD_CPU_LIT_S0 -> +5v
- C130 pad 1: VDD_DDR_S0 -> VDDQ_DDR_S0
- C131 pad 1: VDD_DDR_S0 -> VDDQ_DDR_S0
- C132 pad 1: VDD2_DDR_S3 -> VDDQ_DDR_S0
- C133 pad 1: VCCA_1V8_S0 -> VDDQ_DDR_S0
- C134 pad 1: VDDA_DDR_PLL_S0 -> VDD_DDR_S0
- C135 pad 1: VDDA_0V85_S0 -> VDD_DDR_S0
- C136 pad 1: VDDA_0V85_S0 -> VDD_DDR_S0
- C137 pad 1: VCCA_1V8_S0 -> VDD_DDR_S0
- C138 pad 1: VCCA_1V8_S0 -> VDD_DDR_S0
- C139 pad 1: VDDA_1V2_S0 -> VDD_DDR_S0
- C14 pad 1: VDD_CPU_LIT_S0 -> VDD_NPU_S0
- C140 pad 1: VCCA_1V8_S0 -> VDD2_DDR_S3
- C141 pad 1: Net-(U2UFS-OSC_UFS_XOUT) -> VCCA_1V8_S0
- C142 pad 1: Net-(C142-Pad1) -> VDDA_DDR_PLL_S0
- C143 pad 1: VCCIO_SD_S0 -> VDDA_0V85_S0
- C144 pad 1: VDDA0V75_HDMI_S0 -> VDDA_0V85_S0
- C145 pad 1: VDDA0V75_HDMI_S0 -> VCCA_1V8_S0
- C147 pad 1: VCCA_1V8_S0 -> VDDA_1V2_S0
- C148 pad 1: VDDA_0V75_S0 -> VCCA_1V8_S0
- C149 pad 1: VDDA_0V75_S0 -> Net-(U3UFS-OSC_UFS_XOUT)
- C15 pad 1: VDD_CPU_LIT_S0 -> VDD_NPU_S0
- C150 pad 1: VDDA_1V2_S0 -> Net-(C150-Pad1)
- C151 pad 1: VCCA_1V8_S0 -> VCCIO_SD_S0
- C152 pad 1: Net-(U2MIPI-MIPI_DCPHY_VREG) -> VDDA0V75_HDMI_S0
- C153 pad 1: VDDA_0V75_S0 -> VDDA0V75_HDMI_S0
- C154 pad 1: VDDA_0V75_S0 -> VCCA_1V8_S0
- C158 pad 1: VCCA_1V8_S0 -> VDDA_1V2_S0
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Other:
- board outline added: 2.2 x 8.1 mm
